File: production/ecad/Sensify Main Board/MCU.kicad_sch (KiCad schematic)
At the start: 40 parts, among them J4 1332645, J5 0532611271, J6 Screw_Terminal_01x08, Q6 AO3400A, Q7 AO3400A, SW2 SW_Push, SW3 SW_Push, U5 ESP32-WROOM-32E-N16, U6 CP2102N-A02-GQFN28

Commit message: Updated MCU Schematic
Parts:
- renumbered C27 to C24, C28 to C25, C29 to C26, C30 to C27, C31 to C28, C32 to C29, J4 to J3, J5 to J4, J6 to J5, Q6 to Q5, Q7 to Q6, R22 to R25, R23 to R26, R24 to R27, R25 to R28, R26 to R29, R27 to R30, R28 to R31, R29 to R32, R30 to R33, R31 to R34, R32 to R35, R33 to R36, R34 to R37, R35 to R38, R36 to R39, R37 to R40, R38 to R41, R39 to R42, R40 to R43, R41 to R44, R42 to R45, R43 to R46, SW2 to SW1, SW3 to SW2
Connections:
- net MCU_WAKEUP renamed BMS_ALERT

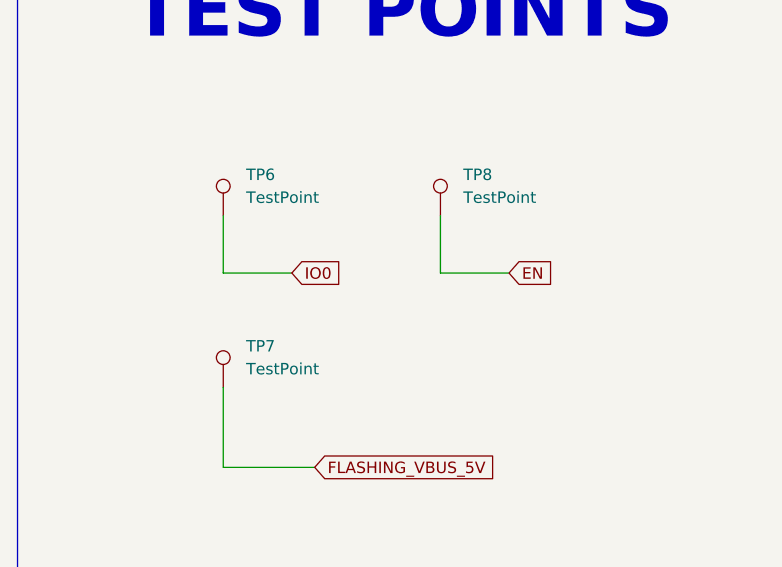
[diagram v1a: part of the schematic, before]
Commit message: Added Labels to Test Points
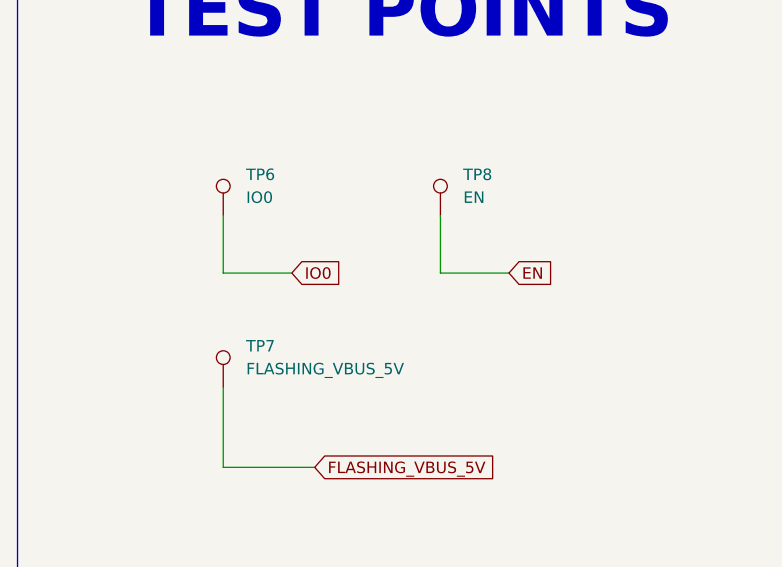
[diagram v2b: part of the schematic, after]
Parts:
- R43, R44: footprint (none) -> Resistor_SMD:R_01005_0402Metric
- TP6: value TestPoint -> IO0
- TP7: value TestPoint -> FLASHING_VBUS_5V
- TP8: value TestPoint -> EN
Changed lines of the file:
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@@
       (effects (font (size 1.27 1.27)))
     )
-    (property "Footprint" "" (at 271.78 188.722 90)
+    (property "Footprint" "Resistor_SMD:R_01005_0402Metric" (at 271.78 188.722 90)
       (effects (font (size 1.27 1.27)) hide)
     )
@@
       (effects (font (size 1.27 1.27)) (justify left))
     )
-    (property "Value" "TestPoint" (at 353.06 215.138 0)
+    (property "Value" "FLASHING_VBUS_5V" (at 353.06 215.138 0)
       (effects (font (size 1.27 1.27)) (justify left))
     )
@@
       (effects (font (size 1.27 1.27)) (justify left))
     )
-    (property "Value" "TestPoint" (at 377.19 196.088 0)
+    (property "Value" "EN" (at 377.19 196.088 0)
       (effects (font (size 1.27 1.27)) (justify left))
     )
@@
       (effects (font (size 1.27 1.27)))
     )
-    (property "Footprint" "" (at 293.37 191.262 90)
+    (property "Footprint" "Resistor_SMD:R_01005_0402Metric" (at 293.37 191.262 90)
       (effects (font (size 1.27 1.27)) hide)
     )
@@
       (effects (font (size 1.27 1.27)) (justify left))
     )
-    (property "Value" "TestPoint" (at 353.06 196.088 0)
-      (effects (font (size 1.27 1.27)) (justify left))
-    )
+    (property "Value" "IO0" (at 353.06 196.088 0)
+      (effects (font (size 1.27 1.27)) (justify left))
+    )

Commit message: Changed Resisitor Footprints
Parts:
- R41, R42, R43, R44: footprint Resistor_SMD:R_01005_0402Metric -> Resistor_SMD:R_0402_1005Metric
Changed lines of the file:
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@@
       (effects (font (size 1.27 1.27)) (justify left))
     )
-    (property "Footprint" "Resistor_SMD:R_01005_0402Metric" (at 256.032 175.26 90)
+    (property "Footprint" "Resistor_SMD:R_0402_1005Metric" (at 256.032 175.26 90)
       (effects (font (size 1.27 1.27)) hide)
     )
@@
       (effects (font (size 1.27 1.27)) (justify left))
     )
-    (property "Footprint" "Resistor_SMD:R_01005_0402Metric" (at 245.872 175.26 90)
+    (property "Footprint" "Resistor_SMD:R_0402_1005Metric" (at 245.872 175.26 90)
       (effects (font (size 1.27 1.27)) hide)
     )
@@
       (effects (font (size 1.27 1.27)))
     )
-    (property "Footprint" "Resistor_SMD:R_01005_0402Metric" (at 271.78 188.722 90)
+    (property "Footprint" "Resistor_SMD:R_0402_1005Metric" (at 271.78 188.722 90)
       (effects (font (size 1.27 1.27)) hide)
     )
@@
       (effects (font (size 1.27 1.27)))
     )
-    (property "Footprint" "Resistor_SMD:R_01005_0402Metric" (at 293.37 191.262 90)
-      (effects (font (size 1.27 1.27)) hide)
-    )
+    (property "Footprint" "Resistor_SMD:R_0402_1005Metric" (at 293.37 191.262 90)
+      (effects (font (size 1.27 1.27)) hide)
+    )

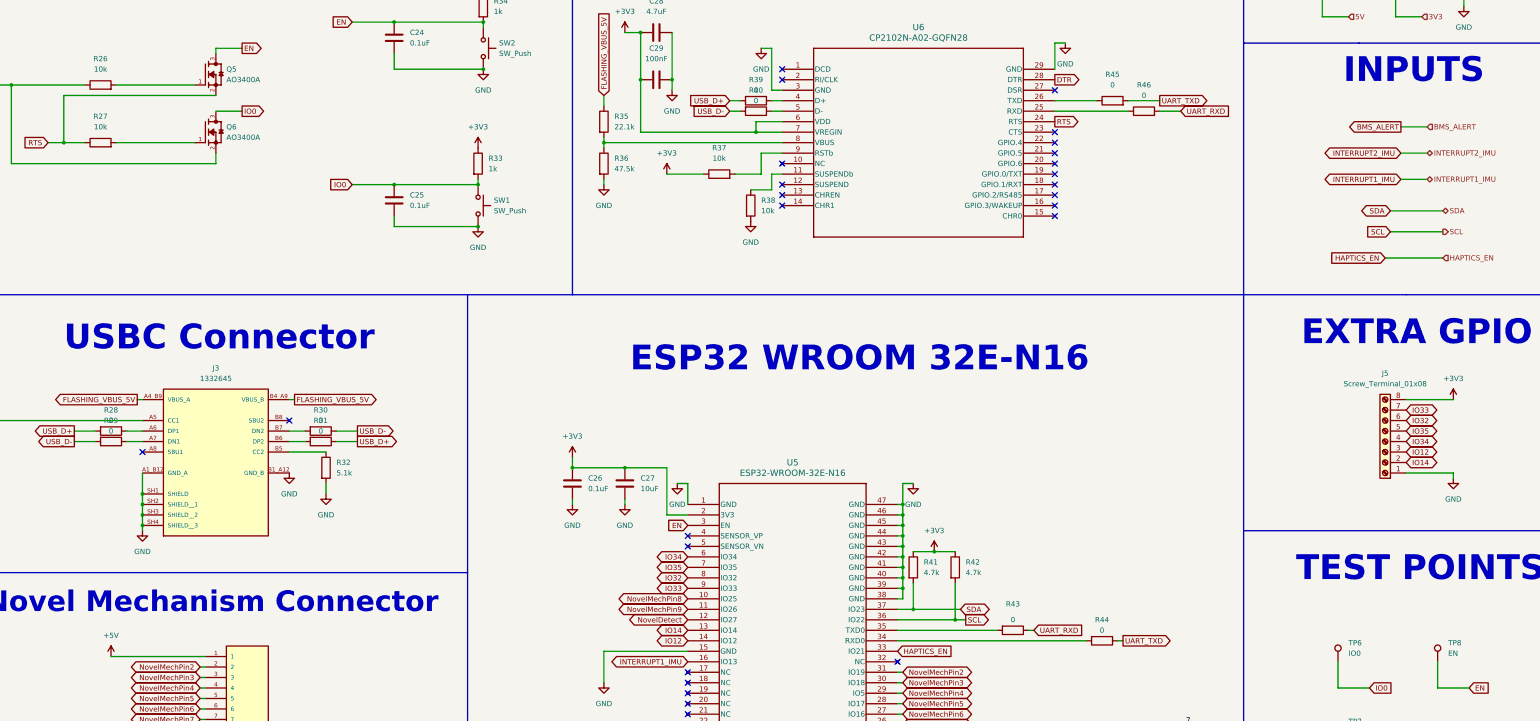
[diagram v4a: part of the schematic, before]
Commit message: UART Routing
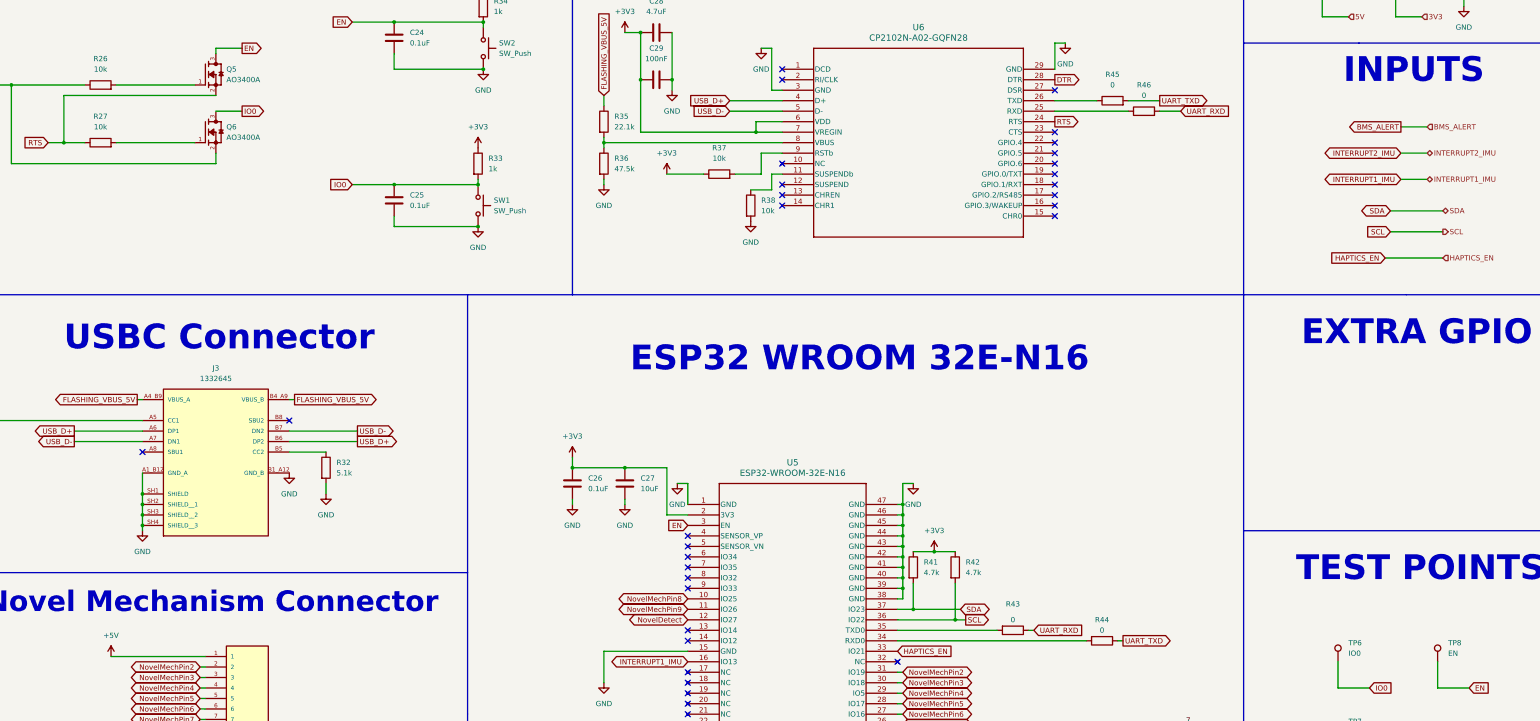
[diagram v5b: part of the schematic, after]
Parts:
- removed J5: Screw_Terminal_01x08, Connector_PinHeader_2.54mm:PinHeader_1x08_P2.54mm_Vertical, symbol Connector:Screw_Terminal_01x08
- removed R28, R29, R30, R31, R39, R40: 0, Resistor_SMD:R_0402_1005Metric, symbol Device:R
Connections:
- net USB_D+: now also J3.A6 (DP1), J3.B6 (DP2), U6.4 (D+)
- net USB_D-: now also J3.A7 (DN1), J3.B7 (DN2), U6.5 (D-)
- net IO12: no longer names the net of U5.14 (IO12)
- net IO14: no longer names the net of U5.13 (IO14)
- net IO32: no longer names the net of U5.8 (IO32)
- net IO33: no longer names the net of U5.9 (IO33)
- net IO34: no longer names the net of U5.6 (IO34)
- net IO35: no longer names the net of U5.7 (IO35)
- no-connect marks 27 -> 33

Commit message: put in TPs + haptics half placed + tried to fit stuff in more
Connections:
- net EN: now also SW2.2; no longer SW2.1
- net GND: now also SW1.1, SW2.1; no longer SW1.2, SW2.2
- net IO0: now also SW1.2; no longer SW1.1
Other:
- moved on the sheet: SW1, SW2
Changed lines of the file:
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@@
   (junction (at 245.11 162.56) (diameter 0) (color 0 0 0 0)
   )
+  (junction (at 245.11 160.02) (diameter 0) (color 0 0 0 0)
+  )
+  (junction (at 76.2 232.41) (diameter 0) (color 0 0 0 0)
+  )
+  (junction (at 245.11 167.64) (diameter 0) (color 0 0 0 0)
+  )
   (junction (at 142.24 92.71) (diameter 0) (color 0 0 0 0)
   )
-  (junction (at 245.11 160.02) (diameter 0) (color 0 0 0 0)
-  )
-  (junction (at 76.2 232.41) (diameter 0) (color 0 0 0 0)
-  )
-  (junction (at 245.11 167.64) (diameter 0) (color 0 0 0 0)
-  )
   (junction (at 60.96 165.1) (diameter 0) (color 0 0 0 0)
   )
@@
   (junction (at 172.72 72.39) (diameter 0) (color 0 0 0 0)
   )
+  (junction (at 143.51 54.61) (diameter 0) (color 0 0 0 0)
+  )
   (junction (at 181.61 45.72) (diameter 0) (color 0 0 0 0)
   )
@@
   )
   (junction (at 60.96 162.56) (diameter 0) (color 0 0 0 0)
-  )
-  (junction (at 143.51 54.61) (diameter 0) (color 0 0 0 0)
   )
   (no_connect (at 193.04 170.18))
@@
     )
   )
-  (symbol (lib_id "Switch:SW_Push") (at 142.24 87.63 270) (unit 1)
-    (in_bom yes) (on_board yes) (dnp no) (fields_autoplaced)
-    (property "Reference" "SW1" (at 146.05 86.36 90)
-      (effects (font (size 1.27 1.27)) (justify left))
-    )
-    (property "Value" "SW_Push" (at 146.05 88.9 90)
-      (effects (font (size 1.27 1.27)) (justify left))
-    )
-    (property "Footprint" "Sensify Footprints:SW_1825910-6-4" (at 147.32 87.63 0)
-      (effects (font (size 1.27 1.27)) hide)
-    )
-    (property "Datasheet" "~" (at 147.32 87.63 0)
+  (symbol (lib_id "Switch:SW_Push") (at 142.24 87.63 90) (unit 1)
+    (in_bom yes) (on_board yes) (dnp no) (fields_autoplaced)
+    (property "Reference" "SW1" (at 143.51 86.36 90)
+      (effects (font (size 1.27 1.27)) (justify right))
+    )
+    (property "Value" "SW_Push" (at 143.51 88.9 90)
+      (effects (font (size 1.27 1.27)) (justify right))
+    )
+    (property "Footprint" "Sensify Footprints:SW_1825910-6-4" (at 137.16 87.63 0)
+      (effects (font (size 1.27 1.27)) hide)
+    )
+    (property "Datasheet" "~" (at 137.16 87.63 0)
       (effects (font (size 1.27 1.27)) hide)
     )
@@
     )
   )
-  (symbol (lib_id "Switch:SW_Push") (at 143.51 49.53 270) (unit 1)
-    (in_bom yes) (on_board yes) (dnp no) (fields_autoplaced)
-    (property "Reference" "SW2" (at 147.32 48.26 90)
-      (effects (font (size 1.27 1.27)) (justify left))
-    )
-    (property "Value" "SW_Push" (at 147.32 50.8 90)
-      (effects (font (size 1.27 1.27)) (justify left))
-    )
-    (property "Footprint" "Sensify Footprints:SW_1825910-6-4" (at 148.59 49.53 0)
-      (effects (font (size 1.27 1.27)) hide)
-    )
-    (property "Datasheet" "~" (at 148.59 49.53 0)
-      (effects (font (size 1.27 1.27)) hide)
-    )
+  (symbol (lib_id "Switch:SW_Push") (at 143.51 49.53 90) (unit 1)
+    (in_bom yes) (on_board yes) (dnp no) (fields_autoplaced)
+    (property "Reference" "SW2" (at 144.78 48.26 90)
+      (effects (font (size 1.27 1.27)) (justify right))
+    )
+    (property "Value" "SW_Push" (at 144.78 50.8 90)
+      (effects (font (size 1.27 1.27)) (justify right))
+    )
+    (property "Footprint" "Sensify Footprints:SW_1825910-6-4" (at 138.43 49.53 0)
+      (effects (font (size 1.27 1.27)) hide)
+    )
+    (property "Datasheet" "~" (at 138.43 49.53 0)
+      (effects (font (size 1.27 1.27)) hide)
+    )

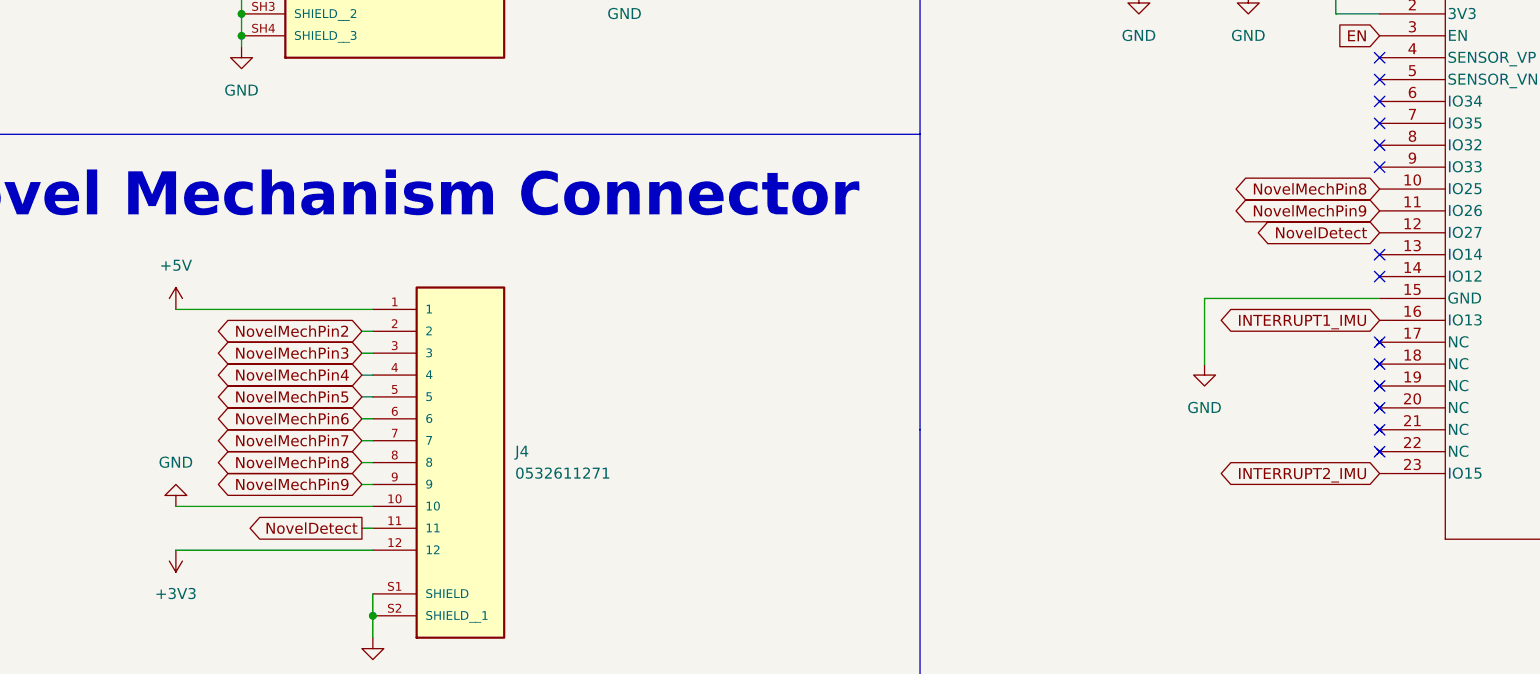
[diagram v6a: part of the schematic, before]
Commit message: Finished UART, Haptics, and IMU
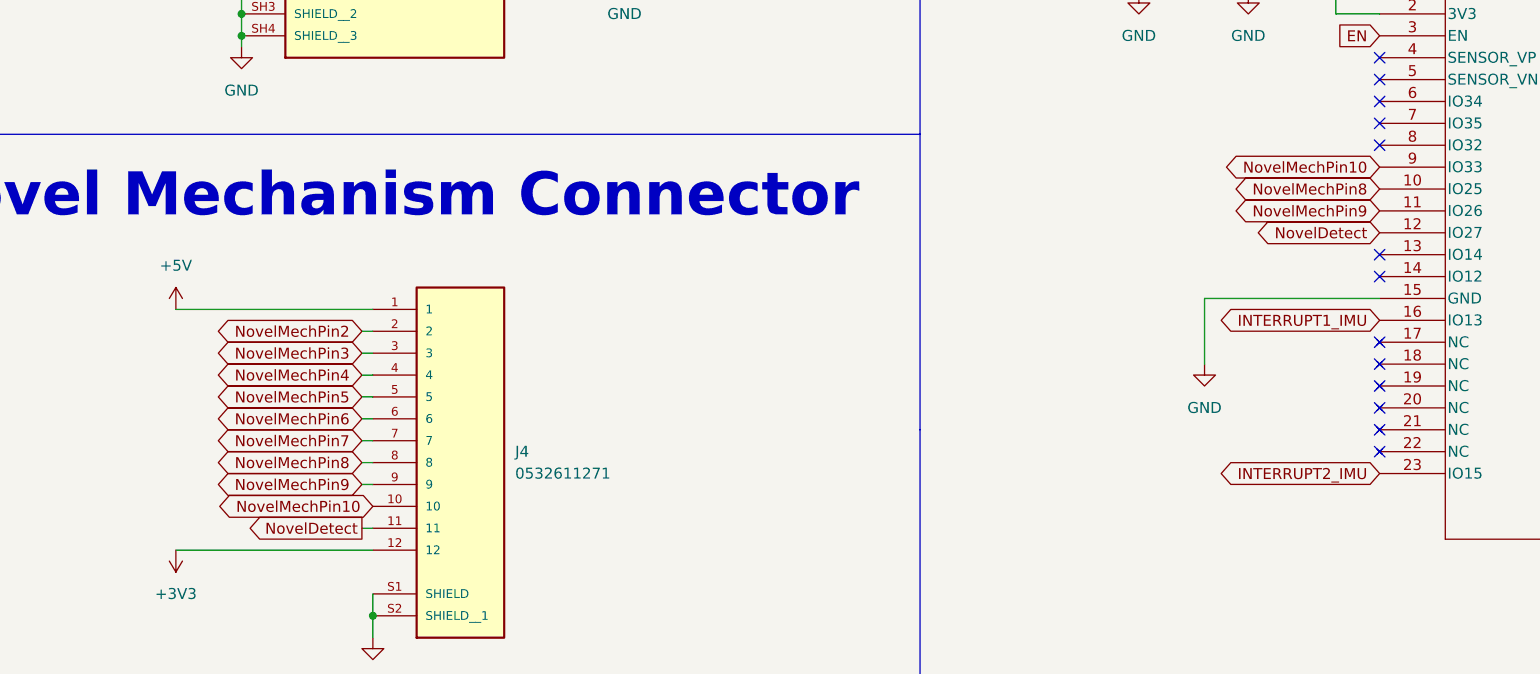
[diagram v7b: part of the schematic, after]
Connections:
- net GND: no longer J4.10
- net NovelMechPin10: now reaches U5.9 (IO33)
- net NovelMechPin10: now also J4.10
- no-connect marks 33 -> 32
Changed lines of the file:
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@@
   (no_connect (at 193.04 203.2))
   (no_connect (at 193.04 213.36))
-  (no_connect (at 193.04 180.34))
   (no_connect (at 243.84 198.12))
   (no_connect (at 281.94 87.63))
@@
     (stroke (width 0) (type default))
   )
-  (wire (pts (xy 53.34 219.71) (xy 76.2 219.71))
-    (stroke (width 0) (type default))
-  )
   (wire (pts (xy 60.96 162.56) (xy 60.96 165.1))
     (stroke (width 0) (type default))
@@
     )
   )
+  (global_label "NovelMechPin10" (shape bidirectional) (at 76.2 219.71 180) (fields_autoplaced)
+    (effects (font (size 1.27 1.27)) (justify right))
+    (property "Intersheetrefs" "${INTERSHEET_REFS}" (at 56.6822 219.71 0)
+      (effects (font (size 1.27 1.27)) (justify right) hide)
+    )
+  )
   (global_label "USB_D-" (shape output) (at 44.45 144.78 180) (fields_autoplaced)
     (effects (font (size 1.27 1.27)) (justify right))
@@
     (property "Intersheetrefs" "${INTERSHEET_REFS}" (at 381.7477 226.06 0)
       (effects (font (size 1.27 1.27)) (justify left) hide)
+    )
+  )
+  (global_label "NovelMechPin10" (shape bidirectional) (at 193.04 180.34 180) (fields_autoplaced)
+    (effects (font (size 1.27 1.27)) (justify right))
+    (property "Intersheetrefs" "${INTERSHEET_REFS}" (at 173.5222 180.34 0)
+      (effects (font (size 1.27 1.27)) (justify right) hide)
     )
   )
@@
         )
       )
-    )
-  )
-  (symbol (lib_id "power:GND") (at 53.34 219.71 180) (unit 1)
-    (in_bom yes) (on_board yes) (dnp no) (fields_autoplaced)
-    (property "Reference" "#PWR057" (at 53.34 213.36 0)
-      (effects (font (size 1.27 1.27)) hide)
-    )
-    (property "Value" "GND" (at 53.34 214.63 0)
-      (effects (font (size 1.27 1.27)))
-    )
-    (property "Footprint" "" (at 53.34 219.71 0)
-      (effects (font (size 1.27 1.27)) hide)
-    )
-    (property "Datasheet" "" (at 53.34 219.71 0)
-      (effects (font (size 1.27 1.27)) hide)
-    )
-    (pin "1")
-    (instances
-      (project "Sensify Main Board"
-        (path "/9a7ba7c3-7d28-4a83-bdbc-38fbff59fcbe/ec3ae12c-a69a-4cda-a73d-a33c865c767e"
-          (reference "#PWR057") (unit 1)
-        )
-      )

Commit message: Added LCSC parts to KiCAD
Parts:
- C23: renamed from C24; LCSC (none) -> C2180807
- C24: renamed from C25; LCSC (none) -> C2180807
- C25: renamed from C26; LCSC (none) -> C2180807
- C26: renamed from C27; LCSC (none) -> C412251
- C27: renamed from C28; LCSC (none) -> C5718966
- C28: renamed from C29; LCSC (none) -> C2180807
- J3: LCSC (none) -> C19193265
- J4: LCSC (none) -> C17393781
- Q5, Q6: LCSC (none) -> C20917
- U5: LCSC (none) -> C701343
- U6: LCSC (none) -> C1550553
- renumbered R25 to R23, R26 to R24, R27 to R25, R32 to R26, R33 to R27, R34 to R28, R35 to R29, R36 to R30, R37 to R31, R38 to R32, R41 to R33, R42 to R34, R43 to R35, R44 to R36, R45 to R37, R46 to R38, SW1 to SW2, SW2 to SW3, TP6 to TP16, TP7 to TP17, TP8 to TP18
